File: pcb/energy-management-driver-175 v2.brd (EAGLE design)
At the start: 151.4 x 34.9 mm, 57 parts, among them T1 BT138-V, T2 BT138-V, T3 BT138-V, T4 BT138-V, T5 BT138-V, T6 BT138-V, T7 BT138-V, T8 BT138-V

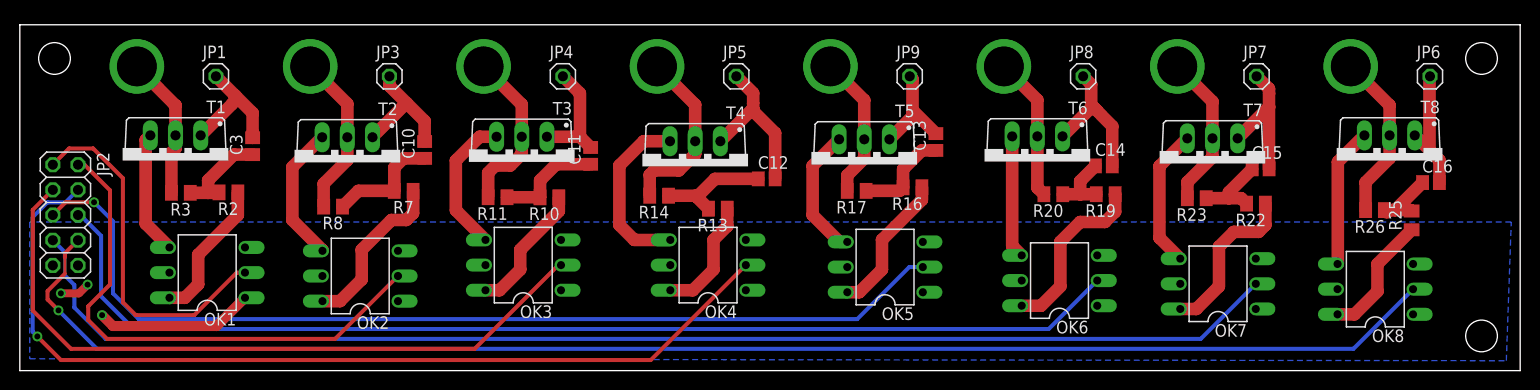
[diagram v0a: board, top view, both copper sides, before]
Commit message: update holes in driver board
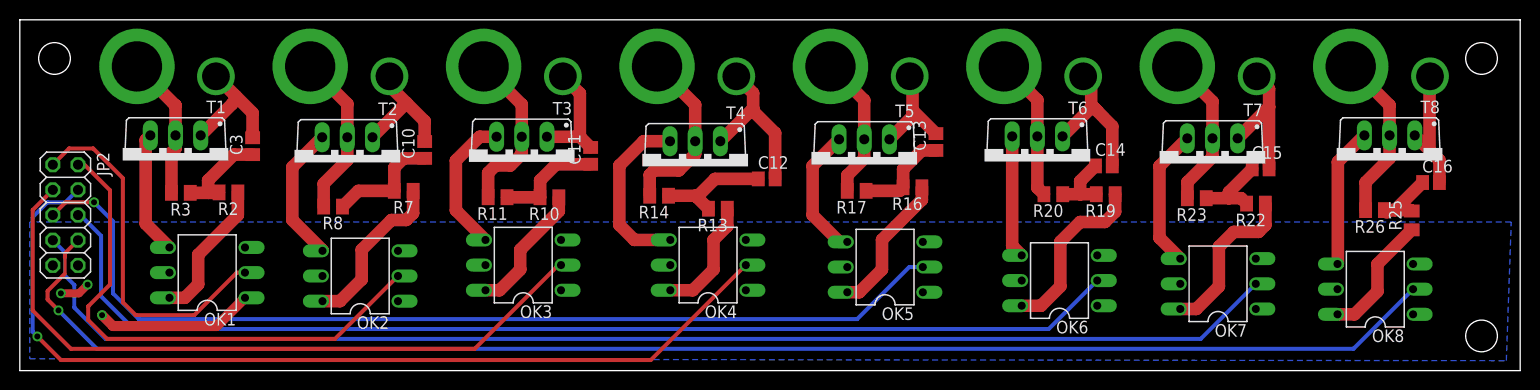
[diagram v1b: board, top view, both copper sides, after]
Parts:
- removed JP1, JP3, JP4, JP5, JP6, JP7, JP8, JP9: (no value), pinhead:1X01
- added U$10, U$11, U$12, U$13, U$14, U$15, U$16, U$9: CONN-CABLE, bontor:CONN-CABLE
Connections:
- net N$15: now also U$11.P$1; no longer JP3.1
- net N$21: now also U$14.P$1; no longer JP4.1
- net N$27: now also U$13.P$1; no longer JP5.1
- net N$33: now also U$10.P$1; no longer JP9.1
- net N$39: now also U$12.P$1; no longer JP8.1
- net N$45: now also U$15.P$1; no longer JP7.1
- net N$51: now also U$16.P$1; no longer JP6.1
- net N$6: now also U$9.P$1; no longer JP1.1
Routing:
- net N$9: vias 1 -> 0
- net N$58: vias 1 -> 0
- net N$57: vias 1 -> 0
- net N$56: vias 1 -> 0
- net N$55: vias 1 -> 0
- net N$54: vias 1 -> 0
- net N$53: vias 1 -> 0
- net N$52: vias 1 -> 0
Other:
- board size 151.4 x 34.9 mm -> 151.4 x 35.4 mm
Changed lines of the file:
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@@
 <setting verticaltext="up"/>
 </settings>
-<grid distance="0.01" unitdist="mm" unit="mm" style="lines" multiple="1" display="no" altdistance="0.01" altunitdist="mm" altunit="mm"/>
+<grid distance="0.5" unitdist="mm" unit="mm" style="lines" multiple="1" display="no" altdistance="0.5" altunitdist="mm" altunit="mm"/>
 <layers>
 <layer number="1" name="Top" color="4" fill="1" visible="yes" active="yes"/>
@@
 <board>
 <plain>
-<wire x1="151.4" y1="1" x2="151.4" y2="35.9" width="0" layer="20"/>
-<wire x1="151.4" y1="35.9" x2="0" y2="35.9" width="0" layer="20"/>
-<wire x1="0" y1="35.9" x2="0" y2="1" width="0" layer="20"/>
+<wire x1="151.4" y1="1" x2="151.4" y2="36.4" width="0" layer="20"/>
+<wire x1="151.4" y1="36.4" x2="0" y2="36.4" width="0" layer="20"/>
+<wire x1="0" y1="36.4" x2="0" y2="1" width="0" layer="20"/>
 <wire x1="0" y1="1" x2="151.4" y2="1" width="0" layer="20"/>
 <hole x="3.5" y="32.5" drill="3.2"/>
@@
 <element name="C16" library="resistor" package="C0805" value="C0.1uF" x="142.4" y="19.98"/>
 <element name="JP2" library="pinhead" package="2X05" value="" x="4.6" y="16.7" rot="R270"/>
-<element name="JP1" library="pinhead" package="1X01" value="" x="19.79" y="30.7"/>
 <element name="U$1" library="bontor" package="CONN-SKUN" value="CONN-SKUN" x="11.82" y="31.7"/>
 <element name="U$2" library="bontor" package="CONN-SKUN" value="CONN-SKUN" x="29.3" y="31.7"/>
@@
 <element name="U$7" library="bontor" package="CONN-SKUN" value="CONN-SKUN" x="99.3" y="31.7"/>
 <element name="U$8" library="bontor" package="CONN-SKUN" value="CONN-SKUN" x="81.8" y="31.7"/>
-<element name="JP3" library="pinhead" package="1X01" value="" x="37.3" y="30.7"/>
-<element name="JP4" library="pinhead" package="1X01" value="" x="54.8" y="30.7"/>
-<element name="JP5" library="pinhead" package="1X01" value="" x="72.3" y="30.7"/>
-<element name="JP6" library="pinhead" package="1X01" value="" x="142.3" y="30.7"/>
-<element name="JP7" library="pinhead" package="1X01" value="" x="124.8" y="30.7"/>
-<element name="JP8" library="pinhead" package="1X01" value="" x="107.3" y="30.7"/>
-<element name="JP9" library="pinhead" package="1X01" value="" x="89.8" y="30.7"/>
+<element name="U$9" library="bontor" package="CONN-CABLE" value="CONN-CABLE" x="19.79" y="30.7"/>
+<element name="U$10" library="bontor" package="CONN-CABLE" value="CONN-CABLE" x="89.8" y="30.71"/>
+<element name="U$11" library="bontor" package="CONN-CABLE" value="CONN-CABLE" x="37.3" y="30.7"/>
+<element name="U$12" library="bontor" package="CONN-CABLE" value="CONN-CABLE" x="107.3" y="30.7"/>
+<element name="U$13" library="bontor" package="CONN-CABLE" value="CONN-CABLE" x="72.3" y="30.7"/>
+<element name="U$14" library="bontor" package="CONN-CABLE" value="CONN-CABLE" x="54.8" y="30.7"/>
+<element name="U$15" library="bontor" package="CONN-CABLE" value="CONN-CABLE" x="124.81" y="30.7"/>
+<element name="U$16" library="bontor" package="CONN-CABLE" value="CONN-CABLE" x="142.3" y="30.7"/>
 </elements>
 <signals>
@@
 <contactref element="T1" pad="T1"/>
 <wire x1="23.49" y1="24.5" x2="23.49" y2="24.9992" width="1.27" layer="1"/>
-<contactref element="JP1" pad="1"/>
 <wire x1="18.25" y1="24.74" x2="21.38176875" y2="27.87176875" width="1.27" layer="1"/>
 <wire x1="23.49" y1="24.5" x2="23.49" y2="27" width="1.27" layer="1"/>
@@
 <wire x1="21.745" y1="28.745" x2="19.79" y2="30.7" width="1.27" layer="1"/>
 <wire x1="21.38176875" y1="27.87176875" x2="21.745" y2="28.745" width="1.27" layer="1" curve="44.82906"/>
+<contactref element="U$9" pad="P$1"/>
 </signal>
 <signal name="N$12">
@@
 <contactref element="C10" pad="2"/>
 <contactref element="T2" pad="T1"/>
-<contactref element="JP3" pad="1"/>
 <wire x1="35.59" y1="24.55" x2="35.59" y2="24.5830875" width="1.27" layer="1"/>
 <wire x1="35.59" y1="24.5830875" x2="39.01918125" y2="28.01226875" width="1.27" layer="1"/>
@@
 <wire x1="39.01918125" y1="28.01226875" x2="37.3" y2="29.73145" width="1.27" layer="1"/>
 <wire x1="37.3" y1="29.73145" x2="37.3" y2="30.7" width="1.27" layer="1"/>
+<contactref element="U$11" pad="P$1"/>
 </signal>
 <signal name="CTRL_SW2">
@@
 <wire x1="57.6" y1="23.52" x2="56.52" y2="24.6" width="1.27" layer="1"/>
 <wire x1="56.52" y1="24.6" x2="53.19" y2="24.6" width="1.27" layer="1"/>
-<contactref element="JP4" pad="1"/>
 <wire x1="54.8" y1="30.7" x2="56.52" y2="28.98" width="1.27" layer="1"/>
 <wire x1="56.52" y1="28.98" x2="56.52" y2="24.6" width="1.27" layer="1"/>
+<contactref element="U$14" pad="P$1"/>
 </signal>
 <signal name="N$24">
@@
 <wire x1="76.22" y1="20.35" x2="76.22" y2="24.98" width="1.27" layer="1"/>
 <wire x1="76.22" y1="24.98" x2="74" y2="27.2" width="1.27" layer="1"/>
-<contactref element="JP5" pad="1"/>
 <wire x1="72.3" y1="30.7" x2="74" y2="29" width="1.27" layer="1"/>
-<wire x1="74" y1="29" x2="74" y2="28" width="1.27" layer="1"/>
+<wire x1="74" y1="29" x2="74" y2="27.46" width="1.27" layer="1"/>
 <wire x1="74" y1="27.46" x2="74" y2="27.2" width="1.27" layer="1"/>
 <wire x1="70.69" y1="24.15" x2="74" y2="27.46" width="1.27" layer="1"/>
-<wire x1="74" y1="27.46" x2="74" y2="28" width="1.27" layer="1"/>
+<contactref element="U$13" pad="P$1"/>
 </signal>
 <signal name="CTRL_SW4">
@@
 <wire x1="87.75" y1="24.34" x2="90.08" y2="26.67" width="1.27" layer="1"/>
 <wire x1="90.08" y1="26.67" x2="90.08" y2="27.28" width="1.27" layer="1"/>
-<contactref element="JP9" pad="1"/>
 <wire x1="90.08" y1="27.28" x2="90.08" y2="30.42" width="1.27" layer="1"/>
+<contactref element="U$10" pad="P$1"/>
 <wire x1="90.08" y1="30.42" x2="89.8" y2="30.7" width="1.27" layer="1"/>
+<wire x1="89.8" y1="30.7" x2="89.8" y2="30.71" width="1.27" layer="1"/>
 </signal>
 <signal name="N$36">
@@
 <wire x1="105.22" y1="24.64" x2="108.110846875" y2="27.530846875" width="1.27" layer="1"/>
 <wire x1="108.110846875" y1="27.530846875" x2="108.405409375" y2="27.530846875" width="1.27" layer="1"/>
-<contactref element="JP8" pad="1"/>
 <wire x1="107.3" y1="30.7" x2="108.110846875" y2="29.889153125" width="1.27" layer="1"/>
 <wire x1="108.110846875" y1="29.889153125" x2="108.110846875" y2="27.530846875" width="1.27" layer="1"/>
+<contactref element="U$12" pad="P$1"/>
 </signal>
 <signal name="N$42">
@@
 <contactref element="T7" pad="T1"/>
 <wire x1="122.89" y1="24.44" x2="122.7692" y2="24.5608" width="1.27" layer="1"/>
-<contactref element="JP7" pad="1"/>
-<wire x1="124.8" y1="30.7" x2="126.06" y2="29.44" width="1.27" layer="1"/>
-<wire x1="126.06" y1="29.44" x2="126.06" y2="29" width="1.27" layer="1"/>
 <wire x1="126.06" y1="27.61" x2="126.06" y2="21.36" width="1.27" layer="1"/>
 <wire x1="122.89" y1="24.44" x2="126.06" y2="27.61" width="1.27" layer="1"/>
-<wire x1="126.06" y1="27.61" x2="126.06" y2="29" width="1.27" layer="1"/>
+<wire x1="126.06" y1="27.61" x2="126.06" y2="29.44" width="1.27" layer="1"/>
+<contactref element="U$15" pad="P$1"/>
+<wire x1="126.06" y1="29.44" x2="124.81" y2="30.69" width="1.27" layer="1"/>
+<wire x1="124.81" y1="30.69" x2="124.81" y2="30.7" width="1.27" layer="1"/>
 </signal>
 <signal name="N$48">
@@
 <wire x1="143.25" y1="22.25" x2="142.25" y2="23.25" width="1.27" layer="1"/>
 <wire x1="142.25" y1="23.25" x2="140.76" y2="24.74" width="1.27" layer="1"/>
-<contactref element="JP6" pad="1"/>
-<wire x1="142.3" y1="30.7" x2="142.25" y2="30.7" width="1.27" layer="1"/>
 <wire x1="142.25" y1="30.7" x2="142.25" y2="23.25" width="1.27" layer="1"/>
+<contactref element="U$16" pad="P$1"/>
+<wire x1="142.25" y1="30.7" x2="142.3" y2="30.7" width="0" layer="19" extent="1-1"/>
 </signal>
 <signal name="CTRL_SW1">
@@
 <wire x1="15.71" y1="27.7754" x2="15.6846" y2="27.7754" width="1.27" layer="1"/>
 <wire x1="15.6846" y1="27.7754" x2="11.82" y2="31.7" width="1.27" layer="1"/>
-<via x="11.8" y="31.7" extent="1-16" drill="4" diameter="5.5"/>
-<wire x1="11.82" y1="31.7" x2="11.8" y2="31.7" width="0" layer="19" extent="1-1"/>
 </signal>
 <signal name="N$52">
@@
 <wire x1="29.3" y1="31.7" x2="30.3" y2="30.6754" width="1.27" layer="1"/>
 <wire x1="30.3" y1="30.6754" x2="33.05" y2="27.9254" width="1.27" layer="1"/>
-<via x="29.3" y="31.7" extent="1-16" drill="4" diameter="5.5"/>
 </signal>
 <signal name="N$53">
@@
 <wire x1="46.8" y1="31.7" x2="47.8054" y2="30.7" width="1.27" layer="1"/>
 <wire x1="47.8054" y1="30.7" x2="50.65" y2="27.8554" width="1.27" layer="1"/>
-<via x="46.8" y="31.7" extent="1-16" drill="4" diameter="5.5"/>
 </signal>
 <signal name="N$54">
@@
 <wire x1="64.3" y1="31.7" x2="65.3" y2="30.6854" width="1.27" layer="1"/>
 <wire x1="65.3" y1="30.6854" x2="68.15" y2="27.8354" width="1.27" layer="1"/>
-<via x="64.3" y="31.7" extent="1-16" drill="4" diameter="5.5"/>
 </signal>
 <signal name="N$55">
@@
 <contactref element="U$5" pad="P$2"/>
 <wire x1="134.3" y1="31.7" x2="138.22" y2="27.78" width="1.27" layer="1"/>
-<via x="134.3" y="31.7" extent="1-16" drill="4" diameter="5.5"/>
 </signal>
 <signal name="N$56">
@@
 <contactref element="U$6" pad="P$2"/>
 <wire x1="116.8" y1="31.7" x2="120.35" y2="28.15" width="1.27" layer="1"/>
-<via x="116.8" y="31.7" extent="1-16" drill="4" diameter="5.5"/>
 </signal>
 <signal name="N$57">
@@
 <wire x1="99.3" y1="31.7" x2="100.3" y2="30.6954" width="1.27" layer="1"/>
 <wire x1="100.3" y1="30.6954" x2="102.68" y2="28.3154" width="1.27" layer="1"/>
-<via x="99.3" y="31.7" extent="1-16" drill="4" diameter="5.5"/>
 </signal>
 <signal name="N$58">
@@
 <wire x1="81.8" y1="31.7" x2="82.8054" y2="30.7" width="1.27" layer="1"/>
 <wire x1="82.8054" y1="30.7" x2="85.21" y2="28.2954" width="1.27" layer="1"/>
-<via x="81.8" y="31.7" extent="1-16" drill="4" diameter="5.5"/>
 </signal>
 <signal name="VDC">
